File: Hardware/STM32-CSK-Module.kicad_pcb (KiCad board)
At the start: 2 copper layers, 27 parts, among them J1 Conn_Cortex-JTAG-10, U1 STM32F417VGT, U2 S34ML02G104T

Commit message: Update PPM numbering
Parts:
- added C14, C15, C16, C17: Capacitor, Capacitors:CAPC1608N, F.Cu at (0.00, 0.00)
- added R2, R3: 0, Resistors:RESC1608N, F.Cu at (0.00, 0.00)
- moved U2 0.50 mm to (207.0, 148.6), turned to 90 degrees
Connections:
- net Net-(H1-Pad70) renamed /~RESET
- net Net-(H1-Pad81) renamed /~ON_SD
- C1 pad 1: /VDDA -> /VREF
- H1 pad 1: Net-(H1-Pad1) -> /I2C3_SDA
- H1 pad 17: Net-(H1-Pad17) -> /USART1_CTS
- H1 pad 19: Net-(H1-Pad19) -> /USART1_RTS
- H1 pad 21: Net-(H1-Pad21) -> /USART2_CTS
- H1 pad 23: Net-(H1-Pad23) -> /USART2_RTS
- H1 pad 25: Net-(H1-Pad25) -> /SPI2_SCK
- H1 pad 27: Net-(H1-Pad27) -> /SPI2_MISO
- H1 pad 29: Net-(H1-Pad29) -> /SPI2_MOSI
- H1 pad 3: Net-(H1-Pad3) -> /I2C3_SCL
- H1 pad 31: Net-(H1-Pad31) -> /~SPI2_SS
- H1 pad 33: Net-(H1-Pad33) -> /USART1_RX
- H1 pad 35: Net-(H1-Pad35) -> /USART1_TX
- H1 pad 37: Net-(H1-Pad37) -> /USART2_RX
- H1 pad 39: Net-(H1-Pad39) -> /USART2_TX
- H1 pad 41: Net-(H1-Pad41) -> /SPI1_SCK
- H1 pad 43: Net-(H1-Pad43) -> /SPI1_MISO
- H1 pad 45: Net-(H1-Pad45) -> /SPI1_MOSI
- H1 pad 47: Net-(H1-Pad47) -> /~SPI1_SS
- H1 pad 5: Net-(H1-Pad5) -> /I2C2_SDA
- H1 pad 55: Net-(H1-Pad55) -> +3V3
- H1 pad 56: Net-(H1-Pad56) -> +3V3
- H1 pad 59: Net-(H1-Pad59) -> GNDA
- H1 pad 60: Net-(H1-Pad60) -> GNDA
- H1 pad 65: Net-(H1-Pad65) -> /VREF
- H1 pad 7: Net-(H1-Pad7) -> /I2C2_SCL
- H1 pad 74: Net-(H1-Pad74) -> /I2C1_SDA
- H1 pad 76: Net-(H1-Pad76) -> /I2C1_SCL
- U1 pad 21: /VDDA -> /VREF
- U1 pad 60: Net-(U1-Pad60) -> /~FSMC_WP
- U2 pad 19: Net-(U2-Pad19) -> /~FSMC_WP

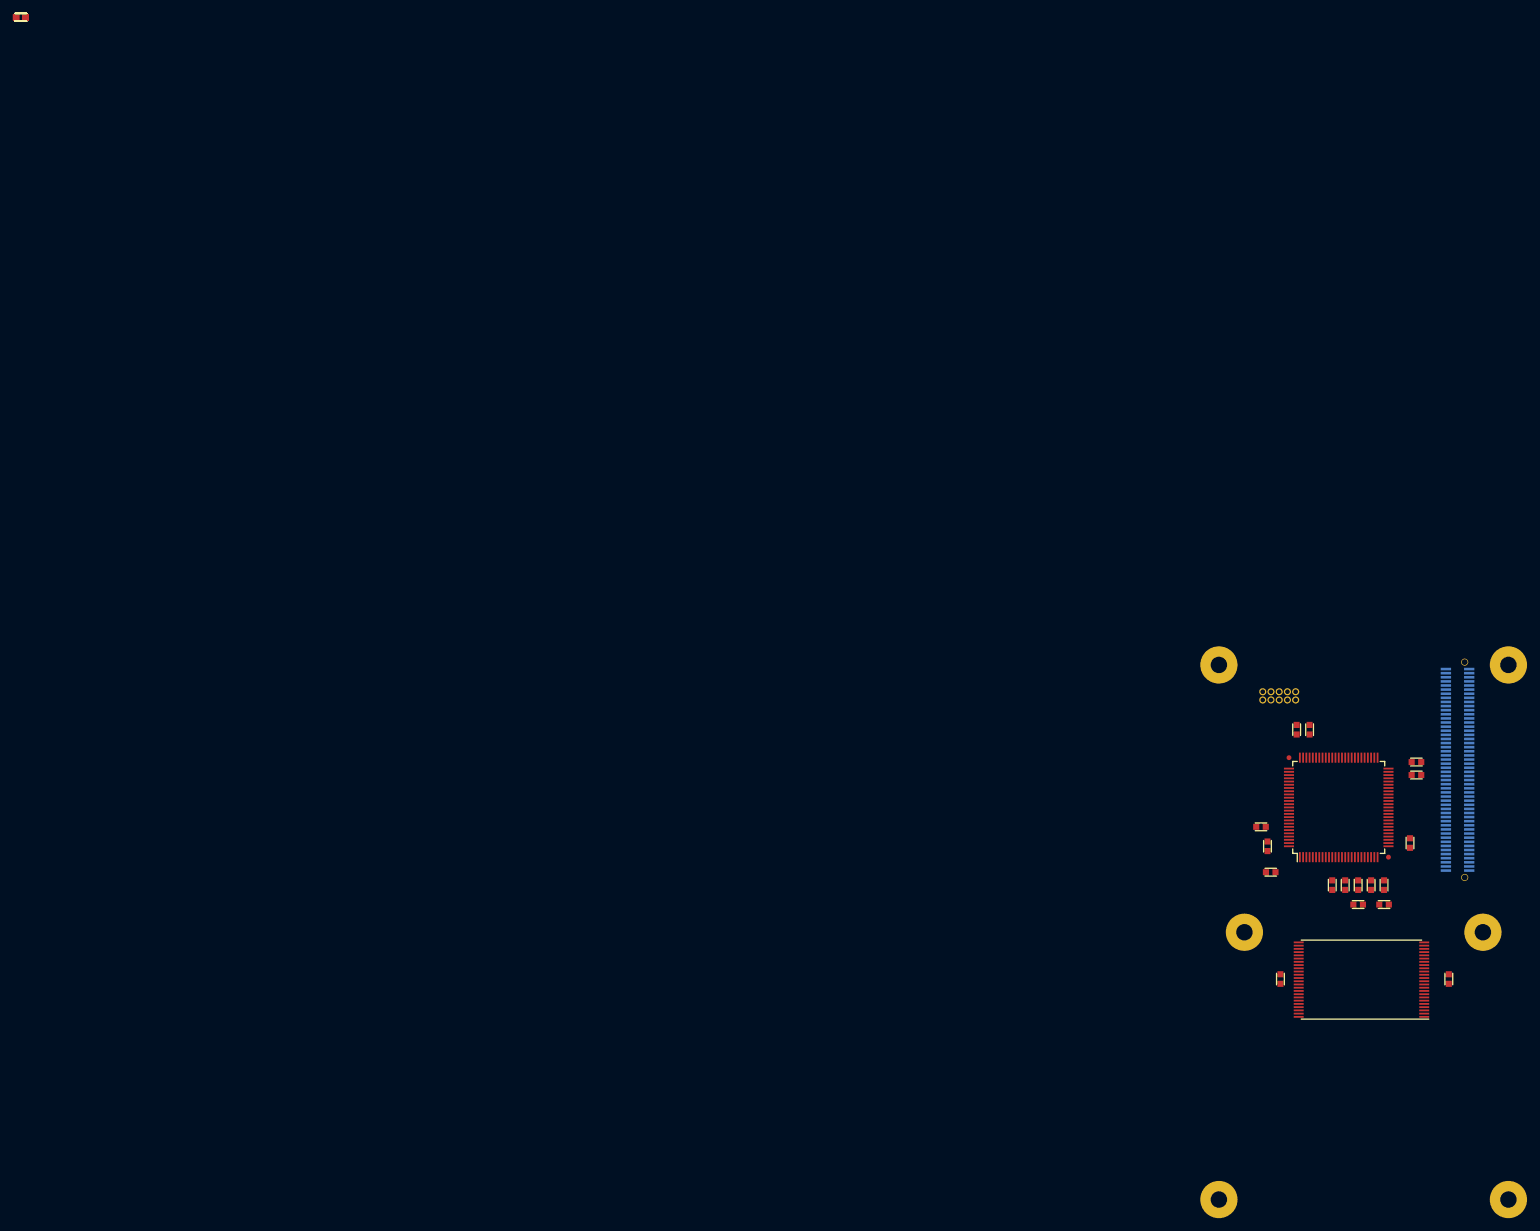
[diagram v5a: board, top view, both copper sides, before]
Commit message: Began routing without external flash
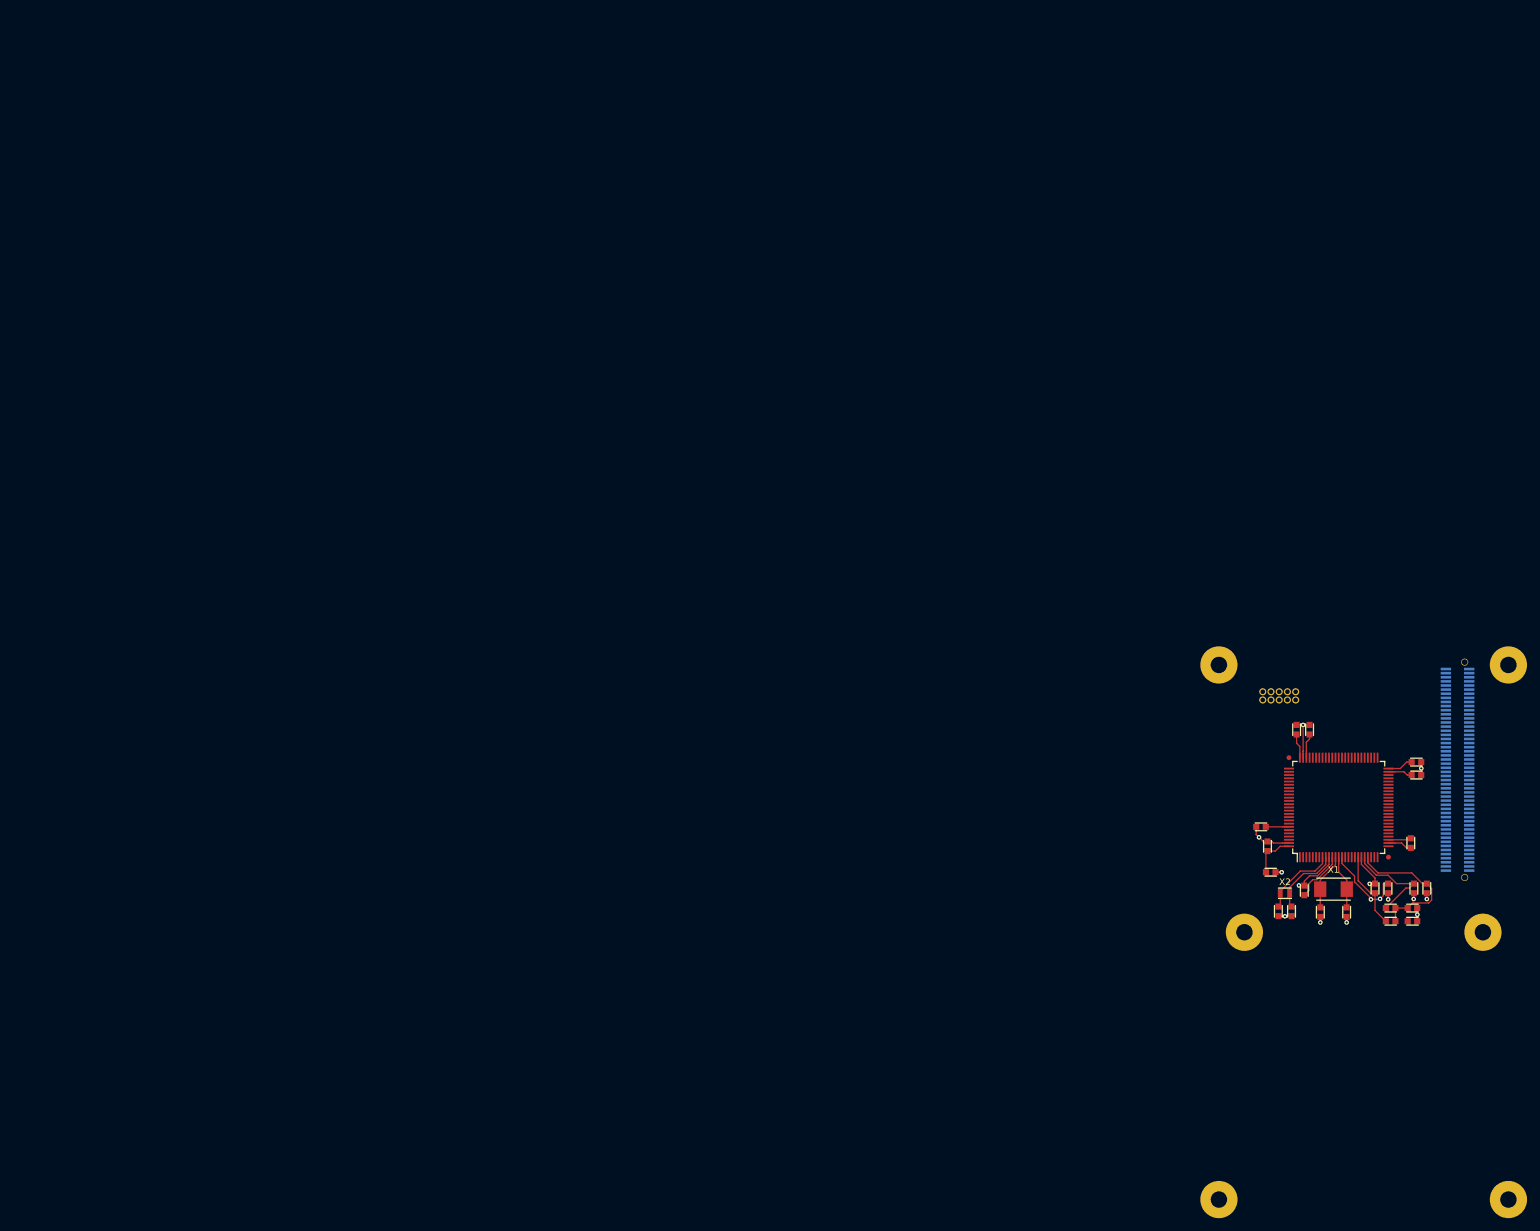
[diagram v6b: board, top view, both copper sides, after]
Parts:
- removed C18, C19: 0.1uF, Capacitors:CAPC1608N
- removed U2: S34ML02G104T, SOP:SOP50P2000-48N
- added X1: 8MHz, Clocks:Crystal_Abracon-ABM3, F.Cu at (202.7, 134.6)
- added X2: 32.768kHz, Clocks:Crystal_Abracon-ABS06, F.Cu at (195.2, 135.3)
- moved R3 256.2 mm to (214.9, 139.6), turned to 180 degrees
- moved R2 252.3 mm to (211.5, 137.5)
- moved C15 247.0 mm to (204.7, 138.2), turned to 270 degrees
- moved C14 243.6 mm to (200.7, 138.2), turned to 270 degrees
- moved C17 239.9 mm to (196.2, 138.0), turned to 270 degrees
- moved C16 238.3 mm to (194.2, 138.0), turned to 270 degrees
- moved C6 8.36 mm to (198.2, 134.8), turned to 90 degrees
- moved C1 6.62 mm to (215.1, 134.5)
- moved C2 6.62 mm to (217.1, 134.5)
- moved C5 6.62 mm to (209.1, 134.5), turned to 90 degrees
- moved C7 6.62 mm to (211.1, 134.5)
- moved FB1 5.64 mm to (211.5, 139.6)
- moved C3 4.42 mm to (214.9, 137.5)
- moved C8 0.13 mm to (214.6, 127.5)
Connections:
- net Net-(U1-Pad15) renamed /AN2
- net Net-(U1-Pad16) renamed /AN3
- net Net-(U1-Pad17) renamed /AN4
- net Net-(U1-Pad18) renamed /AN5
- net Net-(U1-Pad33) renamed /AN6
- net Net-(U1-Pad34) renamed /AN7
- net Net-(U1-Pad35) renamed /AN0
- net Net-(U1-Pad36) renamed /AN1
- H1 pad 1: /I2C3_SDA -> Net-(H1-Pad1)
- H1 pad 17: /USART1_CTS -> Net-(H1-Pad17)
- H1 pad 18: Net-(H1-Pad18) -> /USART1_CTS
- H1 pad 19: /USART1_RTS -> Net-(H1-Pad19)
- H1 pad 2: Net-(H1-Pad2) -> /I2C3_SDA
- H1 pad 20: Net-(H1-Pad20) -> /USART1_RTS
- H1 pad 21: /USART2_CTS -> Net-(H1-Pad21)
- H1 pad 22: Net-(H1-Pad22) -> /USART2_CTS
- H1 pad 23: /USART2_RTS -> Net-(H1-Pad23)
- H1 pad 24: Net-(H1-Pad24) -> /USART2_RTS
- H1 pad 25: /SPI2_SCK -> Net-(H1-Pad25)
- H1 pad 26: Net-(H1-Pad26) -> /SPI2_SCK
- H1 pad 27: /SPI2_MISO -> Net-(H1-Pad27)
- H1 pad 28: Net-(H1-Pad28) -> /SPI2_MISO
- H1 pad 29: /SPI2_MOSI -> Net-(H1-Pad29)
- H1 pad 3: /I2C3_SCL -> Net-(H1-Pad3)
- H1 pad 30: Net-(H1-Pad30) -> /SPI2_MOSI
- H1 pad 31: /~SPI2_SS -> Net-(H1-Pad31)
- H1 pad 32: Net-(H1-Pad32) -> /~SPI2_SS
- H1 pad 33: /USART1_RX -> Net-(H1-Pad33)
- H1 pad 34: Net-(H1-Pad34) -> /USART1_RX
- H1 pad 35: /USART1_TX -> Net-(H1-Pad35)
- H1 pad 36: Net-(H1-Pad36) -> /USART1_TX
- H1 pad 37: /USART2_RX -> Net-(H1-Pad37)
- H1 pad 38: Net-(H1-Pad38) -> /USART2_RX
- H1 pad 39: /USART2_TX -> Net-(H1-Pad39)
- H1 pad 4: Net-(H1-Pad4) -> /I2C3_SCL
- H1 pad 40: Net-(H1-Pad40) -> /USART2_TX
- H1 pad 41: /SPI1_SCK -> Net-(H1-Pad41)
- H1 pad 42: Net-(H1-Pad42) -> /SPI1_SCK
- H1 pad 43: /SPI1_MISO -> Net-(H1-Pad43)
- H1 pad 44: Net-(H1-Pad44) -> /SPI1_MISO
- H1 pad 45: /SPI1_MOSI -> Net-(H1-Pad45)
- H1 pad 46: Net-(H1-Pad46) -> /SPI1_MOSI
- H1 pad 47: /~SPI1_SS -> Net-(H1-Pad47)
- H1 pad 48: Net-(H1-Pad48) -> /~SPI1_SS
- H1 pad 5: /I2C2_SDA -> Net-(H1-Pad5)
- H1 pad 6: Net-(H1-Pad6) -> /I2C2_SDA
- H1 pad 65: /VREF -> Net-(H1-Pad65)
- H1 pad 66: Net-(H1-Pad66) -> /VREF
- H1 pad 69: Net-(H1-Pad69) -> /~RESET
- H1 pad 7: /I2C2_SCL -> Net-(H1-Pad7)
- H1 pad 70: /~RESET -> Net-(H1-Pad70)
- H1 pad 73: Net-(H1-Pad73) -> /I2C1_SDA
- H1 pad 74: /I2C1_SDA -> Net-(H1-Pad74)
- H1 pad 75: Net-(H1-Pad75) -> /I2C1_SCL
- H1 pad 76: /I2C1_SCL -> Net-(H1-Pad76)
- H1 pad 8: Net-(H1-Pad8) -> /I2C2_SCL
- H1 pad 81: /~ON_SD -> Net-(H1-Pad81)
- H1 pad 82: Net-(H1-Pad82) -> /~ON_SD
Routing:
- net GND: track 0.00 -> 42.5 mm, vias 0 -> 13
- net +3V3: track 0.00 -> 38.4 mm
- net /VDDA: track 0.00 -> 22.3 mm
- net /VREF: track 0.00 -> 15.8 mm
- net /~RST: track 0.00 -> 13.3 mm, vias 0 -> 2
- net /SOSCI: track 0.00 -> 11.8 mm
- net /SOSCO: track 0.00 -> 11.2 mm
- net /OSCI: track 0.00 -> 8.74 mm
- net /OSCO: track 0.00 -> 8.28 mm
- net /VCAP2: track 0.00 -> 3.79 mm
- net /VCAP1: track 0.00 -> 3.79 mm
- net /BOOT: track 0.00 -> 3.58 mm
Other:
- net class Default: clearance 0.254 -> 0.1524; trace_width 0.254 -> 0.2032; via_dia 0.889 -> 0.71374; via_drill 0.635 -> 0.3302
- rule trace_clearance: 0.254 -> 0.1524
- rule trace_min: 0.254 -> 0.1524
- rule via_min_drill: 0.508 -> 0.3302
- rule via_min_size: 0.889 -> 0.71374

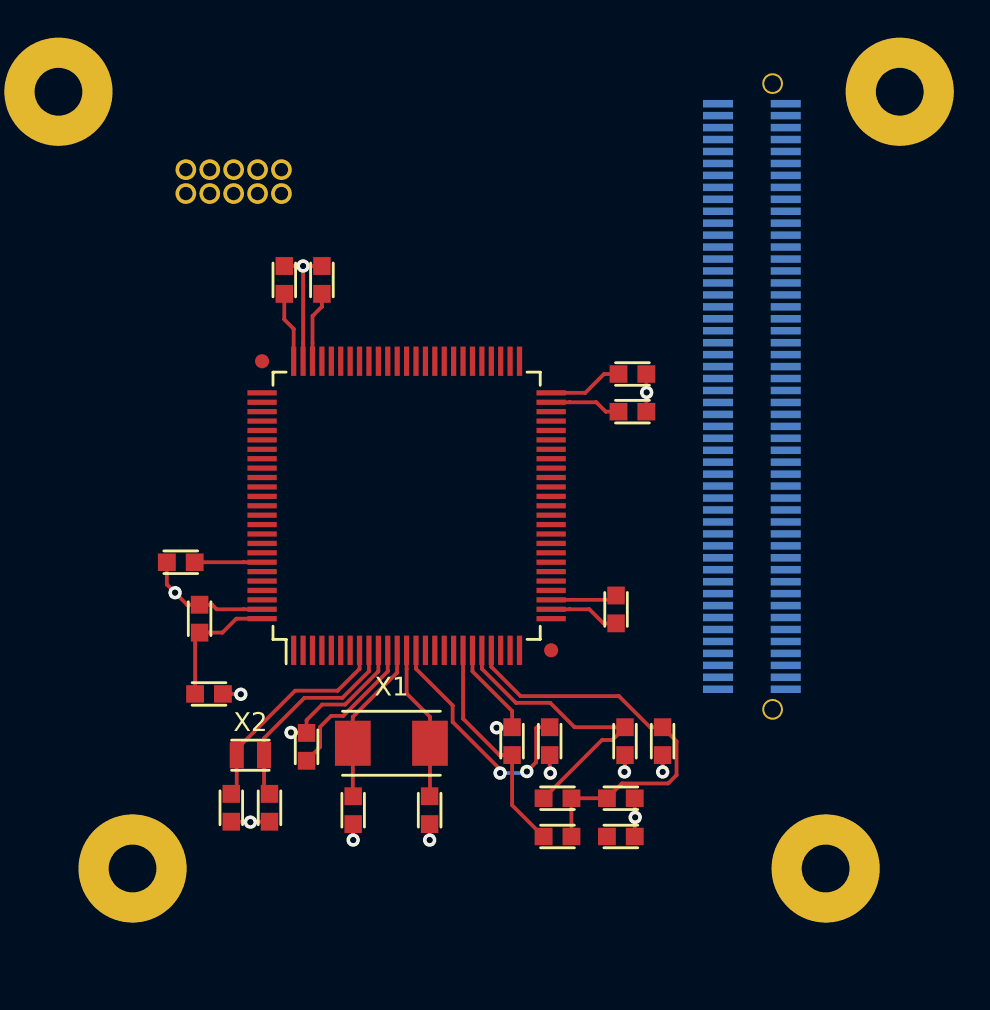
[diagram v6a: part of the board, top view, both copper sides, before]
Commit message: Routed all essentials
All "essential" IO routed, and all power/misc routed as well.
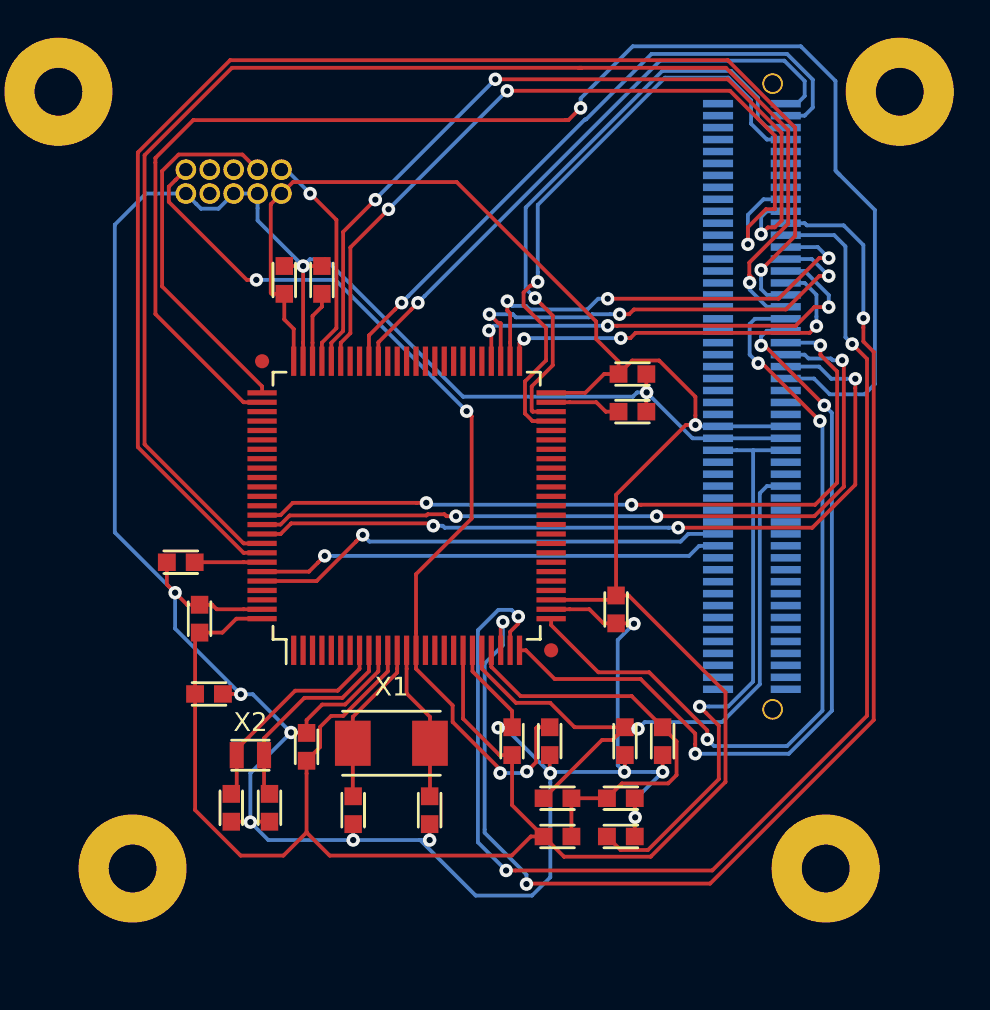
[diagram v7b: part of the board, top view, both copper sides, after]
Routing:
- net GND: track 42.5 -> 169.1 mm, vias 13 -> 14
- net +3V3: track 38.4 -> 146.0 mm, vias 0 -> 1
- net /~SPI1_SS: track 0.00 -> 78.1 mm, vias 0 -> 1
- net /USART1_RX: track 0.00 -> 73.8 mm, vias 0 -> 1
- net /USART1_TX: track 0.00 -> 73.2 mm, vias 0 -> 1
- net /USART2_RTS: track 0.00 -> 69.5 mm, vias 0 -> 3
- net /USART2_CTS: track 0.00 -> 68.9 mm, vias 0 -> 3
- net /USART1_CTS: track 0.00 -> 43.8 mm, vias 0 -> 3
- net /USART2_TX: track 0.00 -> 43.4 mm, vias 0 -> 3
- net /USART1_RTS: track 0.00 -> 43.4 mm, vias 0 -> 3
- net /USART2_RX: track 0.00 -> 42.8 mm, vias 0 -> 3
- net /SPI1_MOSI: track 0.00 -> 42.4 mm, vias 0 -> 3
- net /SPI1_MISO: track 0.00 -> 41.7 mm, vias 0 -> 3
- net /SPI1_SCK: track 0.00 -> 41.0 mm, vias 0 -> 3
- net /~RST: track 13.3 -> 49.8 mm, vias 2 -> 4
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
